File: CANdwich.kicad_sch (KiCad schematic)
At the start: 43 parts, among them J3 DE9_Receptacle, J4 Conn_01x04_Socket, J4 Conn_02x05_Odd_Even, J5 USB_C_Receptacle_USB2.0, U1 AP2127K-3.3, U2 STM32F072CBT6, U3 SN6505BDBV, U5 AP2204RA-5.0, U6 ISO1050DUB, Y1 16MHz

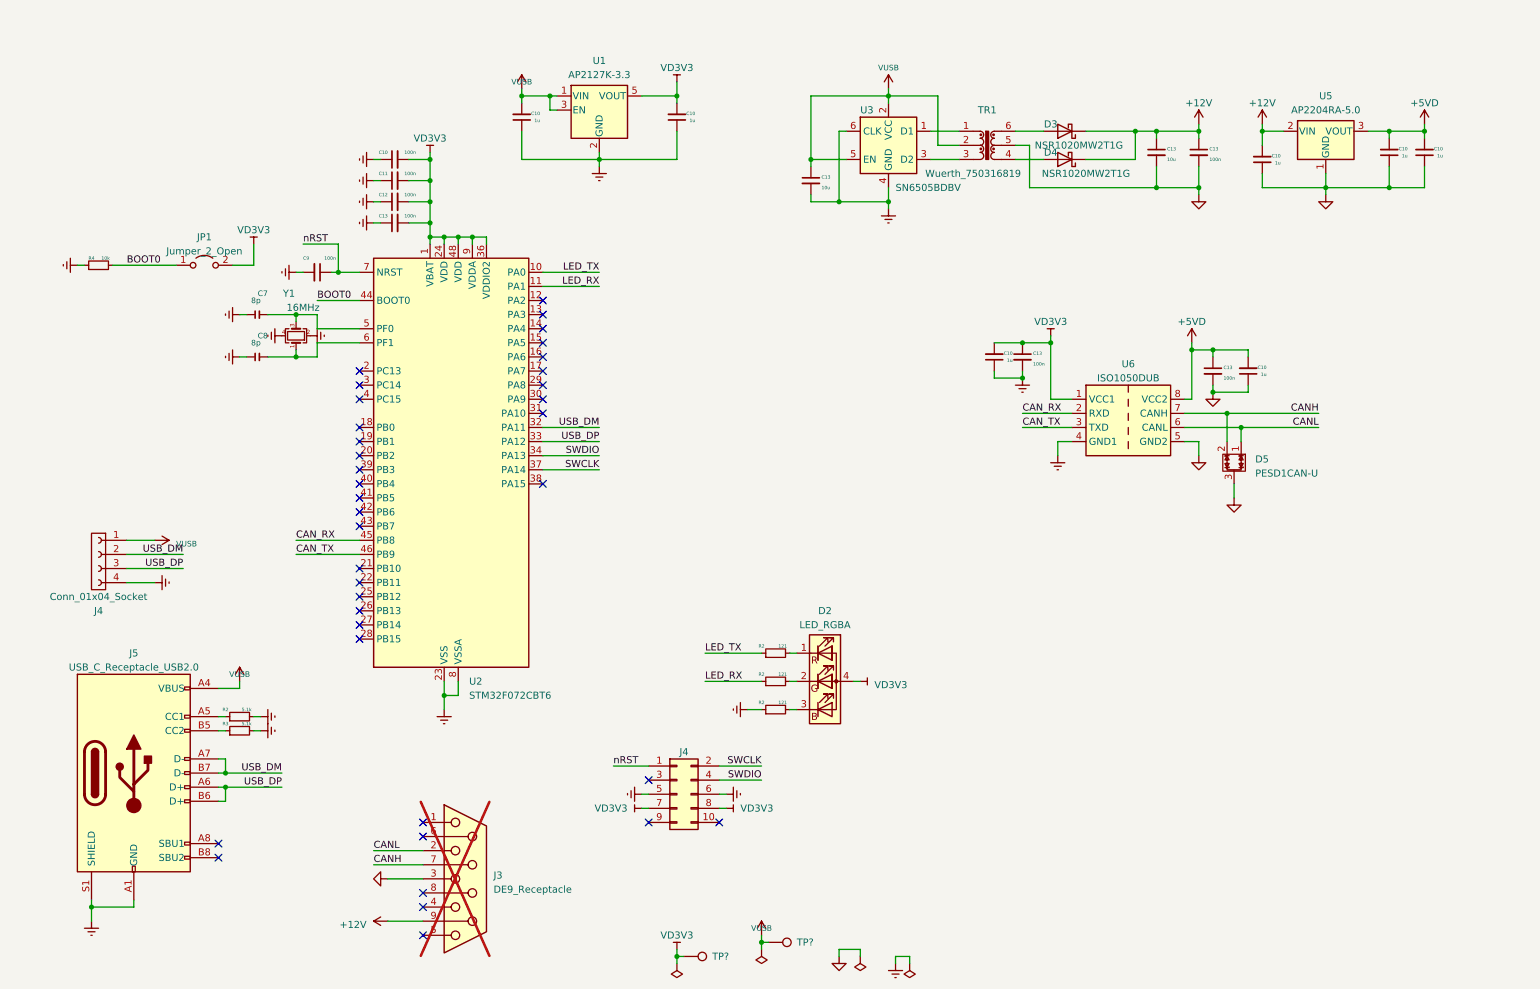
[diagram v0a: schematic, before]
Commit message: Placement in KICAD V7.0.5
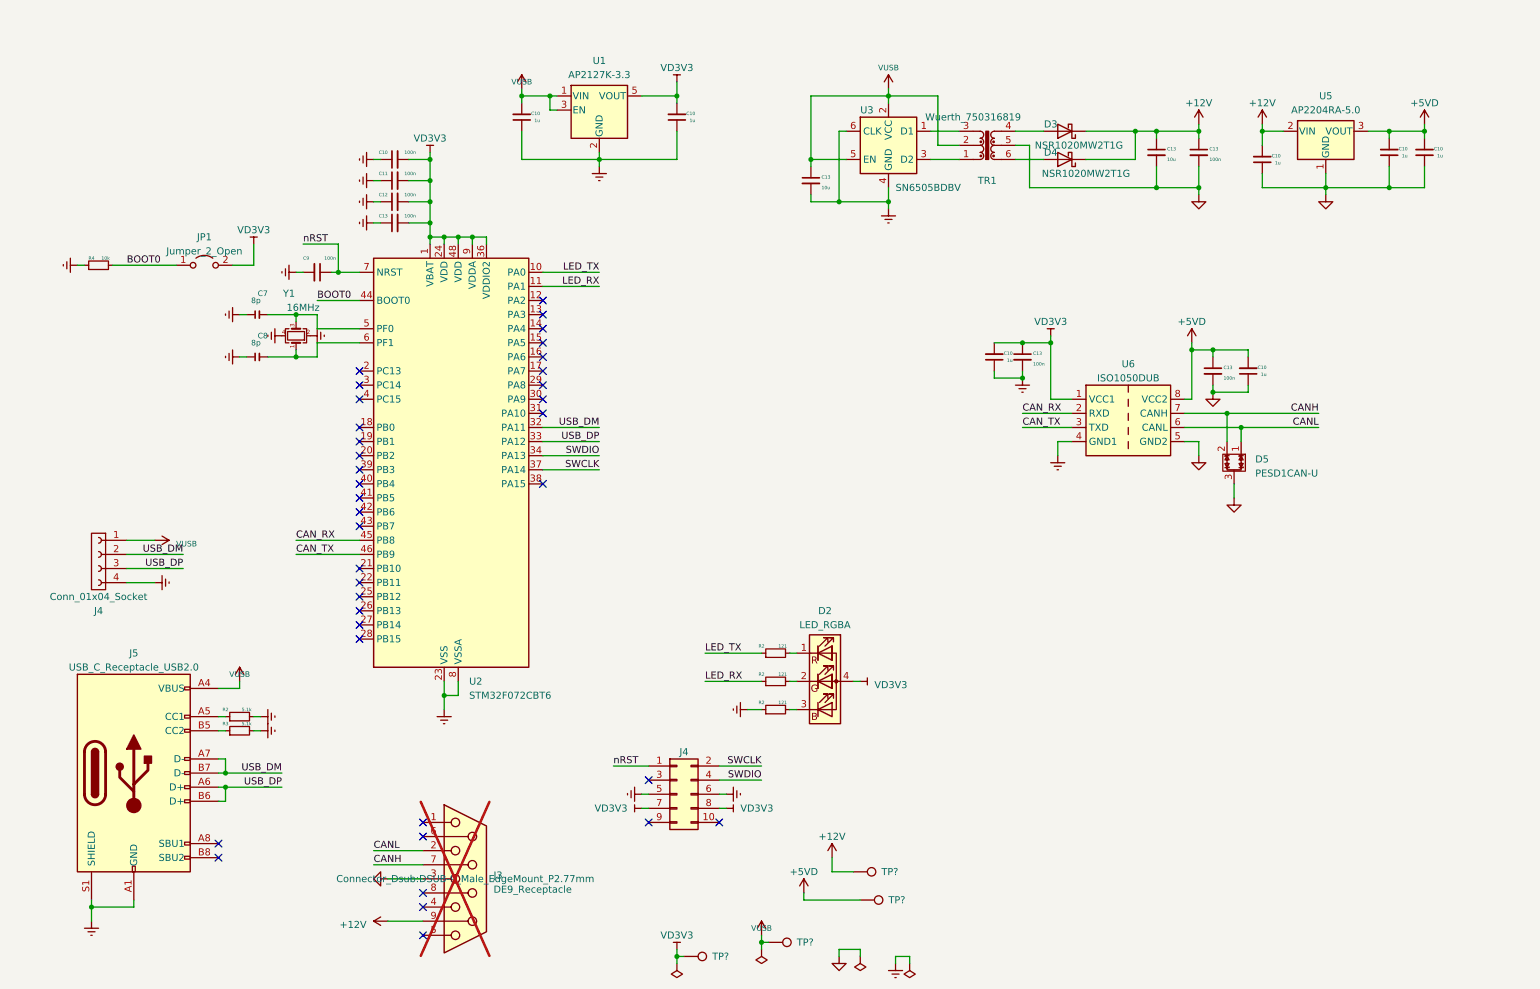
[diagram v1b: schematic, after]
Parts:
- added TP? (x2): TestPoint, TestPoint:TestPoint_Pad_D1.5mm, symbol Connector:TestPoint
- J3: footprint Connector_Dsub:DSUB-9_Female_EdgeMount_P2.77mm -> Connector_Dsub:DSUB-9_Male_EdgeMount_P2.77mm
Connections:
- net +12V: now also TP?.1
- net +5VD: now also TP?.1
- net at D3.2 (A): now also TR1.4; no longer TR1.6
- net at D4.2 (A): now also TR1.6; no longer TR1.4
- net at TR1.1: now also U3.3 (D2); no longer U3.1 (D1)
- net at TR1.3: now also U3.1 (D1); no longer U3.3 (D2)
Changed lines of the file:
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@@
     (stroke (width 0) (type default))
   )
+  (wire (pts (xy 161.29 176.53) (xy 165.1 176.53))
+    (stroke (width 0) (type default))
+  )
   (wire (pts (xy 25.4 67.31) (xy 26.67 67.31))
     (stroke (width 0) (type default))
@@
     (stroke (width 0) (type default))
   )
+  (wire (pts (xy 156.21 181.61) (xy 166.37 181.61))
+    (stroke (width 0) (type default))
+  )
   (wire (pts (xy 200.66 91.44) (xy 204.47 91.44))
     (stroke (width 0) (type default))
@@
     (stroke (width 0) (type default))
   )
+  (wire (pts (xy 156.21 180.34) (xy 156.21 181.61))
+    (stroke (width 0) (type default))
+  )
   (wire (pts (xy 54.61 83.82) (xy 55.88 83.82))
     (stroke (width 0) (type default))
@@
     (stroke (width 0) (type default))
   )
+  (wire (pts (xy 161.29 173.99) (xy 161.29 176.53))
+    (stroke (width 0) (type default))
+  )
   (wire (pts (xy 153.67 147.32) (xy 154.94 147.32))
     (stroke (width 0) (type default))
@@
     )
   )
+  (symbol (lib_id "power:+12V") (at 161.29 173.99 0) (unit 1)
+    (in_bom yes) (on_board yes) (dnp no) (fields_autoplaced)
+    (property "Reference" "#PWR029" (at 161.29 177.8 0)
+      (effects (font (size 1.27 1.27)) hide)
+    )
+    (property "Value" "+12V" (at 161.29 170.18 0)
+      (effects (font (size 1.27 1.27)))
+    )
+    (property "Footprint" "" (at 161.29 173.99 0)
+      (effects (font (size 1.27 1.27)) hide)
+    )
+    (property "Datasheet" "" (at 161.29 173.99 0)
+      (effects (font (size 1.27 1.27)) hide)
+    )
+    (pin "1")
+    (instances
+      (project "CANdwich"
+        (path "/ba121725-8651-4518-b802-e729710bae45"
+          (reference "#PWR029") (unit 1)
+        )
+      )
+    )
+  )
   (symbol (lib_id "power:Earth") (at 171.45 57.15 0) (unit 1)
     (in_bom yes) (on_board yes) (dnp no) (fields_autoplaced)
@@
     )
   )
-  (symbol (lib_id "0_Terry:Wuerth_750316819") (at 189.23 45.72 0) (unit 1)
+  (symbol (lib_id "0_Terry:Wuerth_750316819") (at 189.23 45.72 0) (mirror x) (unit 1)
     (in_bom yes) (on_board yes) (dnp no)
-    (property "Reference" "TR1" (at 189.23 39.37 0)
+    (property "Reference" "TR1" (at 189.23 52.07 0)
       (effects (font (size 1.27 1.27)))
     )
-    (property "Value" "Wuerth_750316819" (at 186.69 50.8 0)
+    (property "Value" "Wuerth_750316819" (at 186.69 40.64 0)
       (effects (font (size 1.27 1.27)))
     )
-    (property "Footprint" "Transformer_SMD:Transformer_Wuerth_750315371" (at 189.23 52.705 0)
+    (property "Footprint" "Transformer_SMD:Transformer_Wuerth_750315371" (at 189.23 38.735 0)
       (effects (font (size 1.27 1.27)) hide)
     )
@@
     )
   )
+  (symbol (lib_id "Connector:TestPoint") (at 166.37 181.61 270) (unit 1)
+    (in_bom no) (on_board yes) (dnp no)
+    (property "Reference" "TP?" (at 171.45 181.61 90)
+      (effects (font (size 1.27 1.27)) (justify left))
+    )
+    (property "Value" "TestPoint" (at 167.767 184.15 0)
+      (effects (font (size 1.27 1.27)) (justify left) hide)
+    )
+    (property "Footprint" "TestPoint:TestPoint_Pad_D1.5mm" (at 166.37 186.69 0)
+      (effects (font (size 1.27 1.27)) hide)
+    )
+    (property "Datasheet" "~" (at 166.37 186.69 0)
+      (effects (font (size 1.27 1.27)) hide)
+    )
+    (property "LCSC" "N/A" (at 166.37 181.61 0)
+      (effects (font (size 1.27 1.27)) hide)
+    )
+    (property "Mfr" "N/A" (at 166.37 181.61 0)
+      (effects (font (size 1.27 1.27)) hide)
+    )
+    (property "PN" "N/A" (at 166.37 181.61 0)
+      (effects (font (size 1.27 1.27)) hide)
+    )
+    (pin "1")
+    (instances
+      (project "LMD016238"
+        (path "/73985f10-d2a2-4be5-a299-a931098bfc12/0075816c-4bf5-4dbf-bca1-25c58ecaeae5"
+          (reference "TP?") (unit 1)
+        )
+        (path "/73985f10-d2a2-4be5-a299-a931098bfc12"
+          (reference "TP13") (unit 1)
+        )
+      )
+      (project "CANdwich"
+        (path "/ba121725-8651-4518-b802-e729710bae45"
+          (reference "TP4") (unit 1)
+        )
+      )
+    )
+  )
   (symbol (lib_id "Device:C_Small") (at 227.33 46.99 0) (unit 1)
     (in_bom yes) (on_board yes) (dnp no)
@@
     )
   )
+  (symbol (lib_id "power:+5VD") (at 156.21 180.34 0) (unit 1)
+    (in_bom yes) (on_board yes) (dnp no) (fields_autoplaced)
+    (property "Reference" "#PWR031" (at 156.21 184.15 0)
+      (effects (font (size 1.27 1.27)) hide)
+    )
+    (property "Value" "+5VD" (at 156.21 176.53 0)
+      (effects (font (size 1.27 1.27)))
+    )
+    (property "Footprint" "" (at 156.21 180.34 0)
+      (effects (font (size 1.27 1.27)) hide)
+    )
+    (property "Datasheet" "" (at 156.21 180.34 0)
+      (effects (font (size 1.27 1.27)) hide)
+    )
+    (pin "1")
+    (instances
+      (project "CANdwich"
+        (path "/ba121725-8651-4518-b802-e729710bae45"
+          (reference "#PWR031") (unit 1)
+        )
+      )
+    )
+  )
   (symbol (lib_id "Connector_Generic:Conn_02x05_Odd_Even") (at 133.35 162.56 0) (unit 1)
     (in_bom yes) (on_board yes) (dnp no) (fields_autoplaced)
@@
       (effects (font (size 1.27 1.27)) (justify left))
     )
-    (property "Footprint" "Connector_Dsub:DSUB-9_Female_EdgeMount_P2.77mm" (at 95.25 177.8 0)
-      (effects (font (size 1.27 1.27)) hide)
+    (property "Footprint" "Connector_Dsub:DSUB-9_Male_EdgeMount_P2.77mm" (at 95.25 177.8 0)
+      (effects (font (size 1.27 1.27)))
     )
     (property "Datasheet" " ~" (at 95.25 177.8 0)
@@
         )
       )
+    )
+  )
+  (symbol (lib_id "Connector:TestPoint") (at 165.1 176.53 270) (unit 1)
+    (in_bom no) (on_board yes) (dnp no)
+    (property "Reference" "TP?" (at 170.18 176.53 90)
+      (effects (font (size 1.27 1.27)) (justify left))
+    )
+    (property "Value" "TestPoint" (at 166.497 179.07 0)
+      (effects (font (size 1.27 1.27)) (justify left) hide)
+    )
+    (property "Footprint" "TestPoint:TestPoint_Pad_D1.5mm" (at 165.1 181.61 0)
+      (effects (font (size 1.27 1.27)) hide)
+    )
+    (property "Datasheet" "~" (at 165.1 181.61 0)
+      (effects (font (size 1.27 1.27)) hide)
+    )
+    (property "LCSC" "N/A" (at 165.1 176.53 0)
+      (effects (font (size 1.27 1.27)) hide)
+    )
+    (property "Mfr" "N/A" (at 165.1 176.53 0)
+      (effects (font (size 1.27 1.27)) hide)
+    )
+    (property "PN" "N/A" (at 165.1 176.53 0)
+      (effects (font (size 1.27 1.27)) hide)
+    )
+    (pin "1")
+    (instances
+      (project "LMD016238"
+        (path "/73985f10-d2a2-4be5-a299-a931098bfc12/0075816c-4bf5-4dbf-bca1-25c58ecaeae5"
+          (reference "TP?") (unit 1)
+        )
+        (path "/73985f10-d2a2-4be5-a299-a931098bfc12"
+          (reference "TP13") (unit 1)
+        )
+      )
+      (project "CANdwich"
+        (path "/ba121725-8651-4518-b802-e729710bae45"
+          (reference "TP3") (unit 1)
+        )
+      )

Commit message: Snapshot for layout
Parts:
- removed C10: 1u, Capacitor_SMD:C_0603_1608Metric, symbol Device:C_Small
- removed J4: Conn_02x05_Odd_Even, Connector_IDC:IDC-Header_2x05_P2.54mm_Vertical_SMD, symbol Connector_Generic:Conn_02x05_Odd_Even
- removed JP1: Jumper_2_Open, Jumper:SolderJumper-2_P1.3mm_Open_Pad1.0x1.5mm, symbol Jumper:Jumper_2_Open
- added R2: 150, Resistor_SMD:R_0603_1608Metric, symbol Device:R_Small
- added TP? (x5): TestPoint, TestPoint:TestPoint_Pad_D1.5mm, symbol Connector:TestPoint
- C10: LCSC C76708 -> C726560; Mfr TDK -> Yageo; PN CGA3E1X7R1E105KT0Y0E -> AC0603KRX7R8BB105
- C10, C11, C12, C13, C9: LCSC C85864 -> C149620; Mfr Murata -> Yageo; PN GCM188R71H104KA57D -> AC0603KRX7R9BB104
- C13: LCSC C86275 -> C109457; Mfr Murata -> Yageo; PN GRM188R61C106KAALD -> CC0603MRX5R7BB106
- J4: now not fitted
- R2: value 121 -> 150; LCSC C170453 -> C114608; Mfr Walsin -> Yageo; PN WR06X1210FTL -> RC0603FR-07150RL
- Y1: footprint Crystal:Crystal_SMD_3225-4Pin_3.2x2.5mm -> Crystal:Crystal_SMD_2520-4Pin_2.5x2.0mm; LCSC C880097 -> C280836; PN NX3225SA-16MHz-STD-CSR-6 -> NX2520SA-16MHZ-STD-CSW-5
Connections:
- net BOOT0: now also R2.1
- net Earth: now also TP?.1
- net GNDA: now also TP?.1
- net SWCLK: now also TP?.1
- net SWDIO: now also TP?.1
- net VD3V3: now also R2.2
- net nRST: now also TP?.1
- net clk_N: now reaches C8.2, U2.6 (PF1), Y1.1
- net clk_P: now reaches C7.2, U2.5 (PF0), Y1.3
- net USB_DM renamed USB_D-
- net USB_DP renamed USB_D+
- no-connect marks 37 -> 34
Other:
- moved on the sheet: C7, C8, R4, Y1
